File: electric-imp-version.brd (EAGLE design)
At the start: 32.1 x 50.8 mm, 44 parts, among them Q1 DMG2307L-7, U1 ELECTRIC_IMP, U2 TPS62172, U3 ATSHA204-TSU, U4 MCP73831, U5 CD74HC4067-SSOPCD74HC4067, U6 CD74HC4067-SSOPCD74HC4067, U7 LTC6904LTC6904, X1 USBSMD

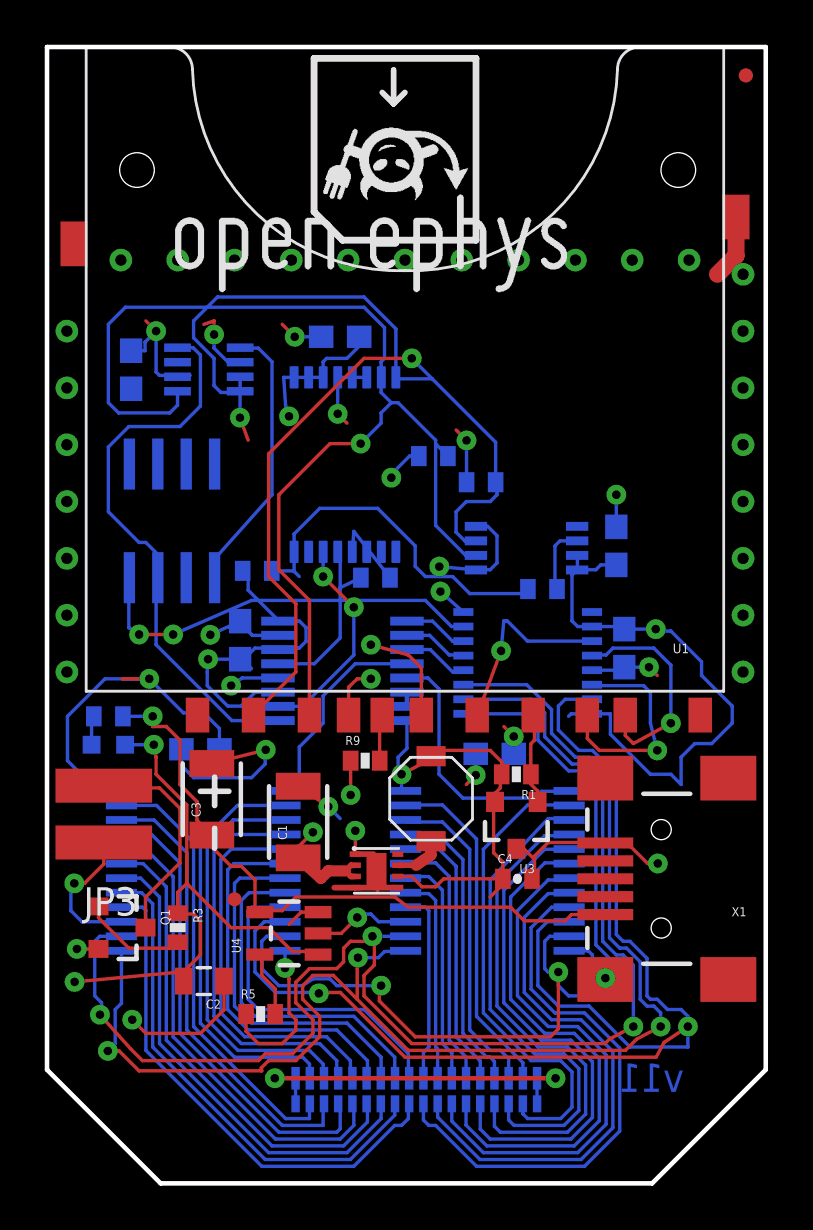
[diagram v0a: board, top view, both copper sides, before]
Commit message: Cleaning up traces
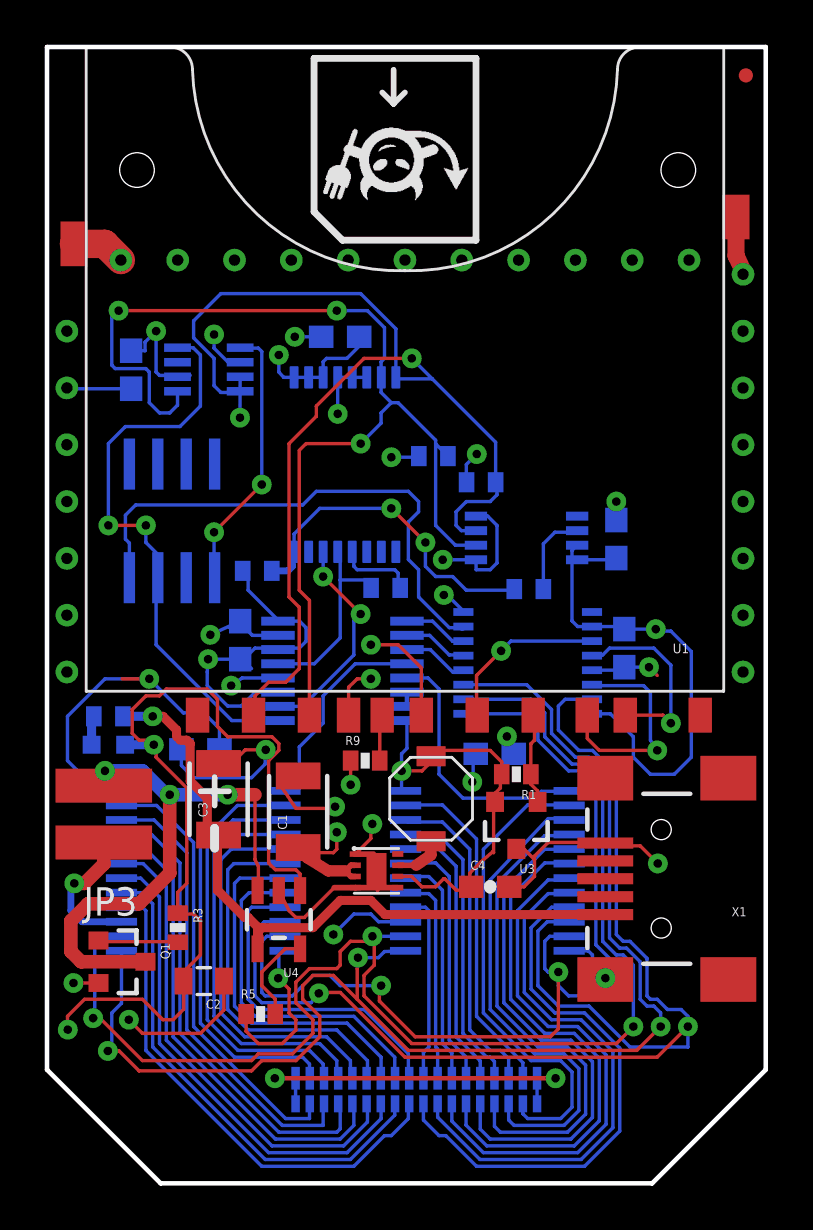
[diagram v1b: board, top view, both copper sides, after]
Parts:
- removed C13: 0.1uF, SparkFun-Capacitors:0603-CAP
- removed JP9: FIDUCIALUFIDUCIAL, SparkFun:MICRO-FIDUCIAL
- added C7: 0.1uF, SparkFun-Capacitors:0603-CAP
- C4: device SparkFun-Passives:0402-CAP -> SparkFun-Capacitors:0603-CAP
- R4: value 330k -> 330
- moved U$5 22.0 mm to (28.2, 28.9)
- moved U$7 20.5 mm to (25.0, 43.9), flipped to the bottom
- moved Q1 1.52 mm to (3.30, 9.91)
- moved C4 1.27 mm to (19.8, 13.3)
- moved U4 0.76 mm to (10.4, 11.8), turned to 180 degrees
- moved R8 0.65 mm to (15.1, 26.6)
- moved R2 0.61 mm to (21.5, 26.6)
- moved C1 0.46 mm to (11.2, 16.6)
- moved U7 0.46 mm to (21.4, 28.9)
- moved C3 0.30 mm to (7.67, 17.2)
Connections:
- net 3.3V: now also C7.1; no longer C13.1
- net GND: now also C7.2; no longer C13.2
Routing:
- net VBAT: track 11.3 -> 26.1 mm, vias 0 -> 3
- net N$9: track 15.2 -> 27.0 mm
- net GND: track 100.6 -> 112.3 mm
- net 3.3V: track 100.0 -> 90.4 mm
- net LM234EN: track 18.1 -> 23.8 mm, vias 2 -> 0
- net VUSB: track 28.9 -> 31.6 mm
- net N$6: track 2.94 -> 4.27 mm
- net VIN: track 22.7 -> 23.9 mm
- net CLOCK: track 16.1 -> 15.0 mm, vias 0 -> 2
- net MUX16_1: track 45.9 -> 47.0 mm
- net RCK: track 9.90 -> 8.76 mm
- net SCK: track 8.73 -> 7.68 mm
- net MUX16_0: track 57.1 -> 58.1 mm
- net CURRENT_SOURCE: track 25.9 -> 26.8 mm, vias 0 -> 2
- net SDA: track 51.2 -> 50.5 mm, vias 1 -> 3
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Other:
- board text added: "autoimpedance, v 2.0"
- board text removed: "GND"
- board text removed: "VIN"

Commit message: Fix layout
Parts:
- removed FRAME1: FRAME-LETTER, SparkFun-Aesthetics:CREATIVE_COMMONS
- moved U2 4.55 mm to (18.2, 11.1)
- moved JP3 3.61 mm to (5.74, 14.8)
- moved C3 2.76 mm to (10.4, 16.9)
- moved R3 2.75 mm to (6.76, 8.84), turned to 0 degrees
- moved C1 2.31 mm to (13.5, 16.9)
- moved L1 2.29 mm to (17.3, 14.9)
- moved C2 2.00 mm to (6.71, 7.06)
- moved Q1 1.84 mm to (3.45, 8.08)
- moved R9 1.59 mm to (15.7, 18.4), turned to 90 degrees
- moved C4 1.37 mm to (21.2, 13.3)
- moved C5 0.15 mm to (20.0, 19.1)
- moved U3 0.15 mm to (21.1, 16.1)
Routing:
- net N$9: track 27.0 -> 12.6 mm
- net VUSB: track 31.6 -> 39.4 mm
- net MUX16_2: track 61.1 -> 68.3 mm
- net MUX16_3: track 61.2 -> 66.7 mm
- net VBAT: track 26.1 -> 20.7 mm, vias 3 -> 0
- net MUX16_1: track 47.0 -> 52.1 mm
- net SCL: track 51.4 -> 54.8 mm
- net VIN: track 23.9 -> 26.7 mm
- net 3.3V: track 90.4 -> 93.2 mm, vias 13 -> 12
- net N$1: track 2.24 -> 4.38 mm
- net N$2: track 3.98 -> 5.96 mm
- net EIB_GND: track 37.1 -> 38.0 mm
- net SCK: track 7.68 -> 8.35 mm
- net GND: track 112.3 -> 112.8 mm, vias 45 -> 44
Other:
- board text added: "autoimpedance 2.0"
- board text removed: "autoimpedance, v 2.0"

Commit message: Aesthetic fixes
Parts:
- removed U4: MCP73831, SparkFun-PowerIC:SOT23-5
- added CHARGE: MCP73831, SparkFun-PowerIC:SOT23-5
- added FRAME1: FRAME-LETTER, SparkFun-Aesthetics:CREATIVE_COMMONS
- moved C7 0.84 mm to (26.3, 28.9)
- moved C3 0.24 mm to (10.6, 16.9)
- moved R6 0.23 mm to (19.2, 31.3)
- moved R5 0.17 mm to (9.40, 7.49)
- moved R8 0.08 mm to (15.1, 26.5)
- renumbered JP3 to JP1, S1 to OMNETICS, U$3 to IC1, U$4 to IC3, U$6 to IC2, U$8 to MUX3X2, U1 to SD, U2 to CONV, U3 to ID, U5 to MUX16A, U6 to MUX16B, U7 to CLK, U8 to SR, X1 to USB
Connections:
- net GND: now also CHARGE.2; no longer U4.2
- net N$6: now also CHARGE.5; no longer U4.5
- net N$9: now also CHARGE.1; no longer U4.1
- net VBAT: now also CHARGE.3; no longer U4.3
- net VUSB: now also CHARGE.4; no longer U4.4
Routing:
- net SDA: track 50.5 -> 44.3 mm
- net 3.3V: track 93.2 -> 95.4 mm
- net VIN: track 26.7 -> 28.2 mm
- net TEST_OUT: track 9.77 -> 11.1 mm
- net VUSB: track 39.4 -> 38.4 mm
- net CLOCK: track 15.0 -> 15.6 mm

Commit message: Aesthetic fixes
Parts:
- moved U$5 32.2 mm to (6.76, 4.90)
- moved Q1 0.61 mm to (2.84, 8.08)
- moved C2 0.46 mm to (6.25, 7.06)
- moved R1 0.30 mm to (21.0, 18.6)
- moved R3 0.15 mm to (6.76, 8.99)
- moved C4 0.08 mm to (21.2, 13.2)
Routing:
- net N$2: track 5.96 -> 6.96 mm
- net GND: track 112.9 -> 113.9 mm
- net 3.3V: track 95.4 -> 96.2 mm
- net VBAT: track 20.9 -> 21.4 mm

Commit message: Fix LM234 channel mapping
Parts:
- removed IC2: LM234, josh:LM234
- added U$2: LM234, josh:LM234
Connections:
- net CURRENT_SOURCE: now also U$2.6; no longer IC2.3
- net LM234EN: now also U$2.4; no longer IC2.4
- net W: now also U$2.1; no longer IC2.1
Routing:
- net CURRENT_SOURCE: track 27.1 -> 30.4 mm, vias 2 -> 0
- net W: track 12.1 -> 13.8 mm
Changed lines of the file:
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@@
 <grid distance="0.003" unitdist="inch" unit="inch" style="lines" multiple="1" display="yes" altdistance="0.005" altunitdist="inch" altunit="inch"/>
 <layers>
-<layer number="1" name="Top" color="4" fill="1" visible="no" active="yes"/>
+<layer number="1" name="Top" color="4" fill="1" visible="yes" active="yes"/>
 <layer number="2" name="Route2" color="11" fill="1" visible="no" active="yes"/>
 <layer number="3" name="Route3" color="8" fill="1" visible="no" active="yes"/>
@@
 <layer number="17" name="Pads" color="2" fill="1" visible="yes" active="yes"/>
 <layer number="18" name="Vias" color="2" fill="1" visible="yes" active="yes"/>
-<layer number="19" name="Unrouted" color="14" fill="1" visible="yes" active="yes"/>
+<layer number="19" name="Unrouted" color="15" fill="1" visible="yes" active="yes"/>
 <layer number="20" name="Dimension" color="15" fill="1" visible="yes" active="yes"/>
 <layer number="21" name="tPlace" color="3" fill="1" visible="no" active="yes"/>
 <layer number="22" name="bPlace" color="5" fill="1" visible="yes" active="yes"/>
-<layer number="23" name="tOrigins" color="15" fill="1" visible="no" active="yes"/>
+<layer number="23" name="tOrigins" color="15" fill="1" visible="yes" active="yes"/>
 <layer number="24" name="bOrigins" color="15" fill="1" visible="yes" active="yes"/>
 <layer number="25" name="tNames" color="3" fill="1" visible="no" active="yes"/>
@@
 <attribute name="VALUE" x="10.7569" y="6.9596" size="0.4064" layer="27" font="vector" ratio="10"/>
 </element>
-<element name="IC2" library="josh" package="LM234" value="LM234" x="5.588" y="29.6164" rot="MR0"/>
 <element name="R6" library="SparkFun-Passives" package="0402-RES" value="4.7k" x="19.177" y="31.3436" smashed="yes" rot="MR0">
 <attribute name="NAME" x="20.1422" y="31.9659" size="0.4064" layer="26" font="vector" ratio="10" rot="MR0"/>
@@
 </element>
 <element name="FRAME1" library="SparkFun-Aesthetics" package="CREATIVE_COMMONS" value="FRAME-LETTER" x="-3.7338" y="-11.7348"/>
+<element name="U$2" library="josh" package="LM234" value="LM234" x="4.7244" y="29.4132" rot="MR0"/>
 </elements>
 <signals>
@@
 </signal>
 <signal name="LM234EN">
-<contactref element="IC2" pad="4"/>
 <contactref element="SR" pad="7"/>
-<wire x1="3.683" y1="27.0764" x2="3.683" y2="28.6258" width="0.1524" layer="16"/>
-<wire x1="3.683" y1="28.6258" x2="3.5052" y2="28.8036" width="0.1524" layer="16"/>
-<wire x1="3.5052" y1="28.8036" x2="3.5052" y2="29.8704" width="0.1524" layer="16"/>
-<wire x1="3.5052" y1="29.8704" x2="3.9624" y2="30.3276" width="0.1524" layer="16"/>
 <wire x1="3.9624" y1="30.3276" x2="11.43" y2="30.3276" width="0.1524" layer="16"/>
 <wire x1="11.43" y1="30.3276" x2="12.0396" y2="30.9372" width="0.1524" layer="16"/>
@@
 <wire x1="17.9832" y1="24.8412" x2="18.5632" y2="24.8412" width="0.1524" layer="16"/>
 <wire x1="18.5632" y1="24.8412" x2="18.6134" y2="24.8914" width="0.1524" layer="16"/>
+<contactref element="U$2" pad="4"/>
+<wire x1="3.9624" y1="30.3276" x2="2.8956" y2="29.2608" width="0.1524" layer="16"/>
+<wire x1="2.8956" y1="29.2608" x2="2.8956" y2="26.9494" width="0.1524" layer="16"/>
+<wire x1="2.8956" y1="26.9494" x2="2.8194" y2="26.8732" width="0.1524" layer="16"/>
 </signal>
 <signal name="W">
 <contactref element="IC3" pad="1"/>
-<contactref element="IC2" pad="1"/>
-<wire x1="7.493" y1="27.0764" x2="7.493" y2="27.9146" width="0.1524" layer="16"/>
-<wire x1="7.493" y1="27.9146" x2="7.4676" y2="27.8892" width="0.1524" layer="16"/>
-<wire x1="7.4676" y1="27.8892" x2="7.4676" y2="29.1084" width="0.1524" layer="16"/>
-<wire x1="7.4676" y1="29.1084" x2="9.6012" y2="31.242" width="0.3048" layer="1"/>
+<wire x1="7.5438" y1="29.4894" x2="9.6012" y2="29.4894" width="0.1524" layer="16"/>
+<wire x1="9.6012" y1="29.4894" x2="9.6012" y2="31.242" width="0.3048" layer="1"/>
 <wire x1="9.6012" y1="31.242" x2="9.6012" y2="37.1856" width="0.1524" layer="16"/>
 <wire x1="9.6012" y1="37.1856" x2="9.4488" y2="37.338" width="0.1524" layer="16"/>
 <wire x1="9.4488" y1="37.338" x2="8.655" y2="37.338" width="0.1524" layer="16"/>
 <wire x1="8.655" y1="37.338" x2="8.6344" y2="37.3586" width="0.1524" layer="16"/>
-<via x="7.4676" y="29.1084" extent="1-16" drill="0.381"/>
+<via x="9.6012" y="29.4894" extent="1-16" drill="0.381"/>
 <via x="9.6012" y="31.242" extent="1-16" drill="0.381"/>
+<contactref element="U$2" pad="1"/>
+<wire x1="6.6294" y1="26.8732" x2="6.6294" y2="28.575" width="0.1524" layer="16"/>
+<wire x1="6.6294" y1="28.575" x2="7.5438" y2="29.4894" width="0.1524" layer="16"/>
 </signal>
 <signal name="CURRENT_SOURCE">
 <contactref element="IC3" pad="8"/>
-<contactref element="IC2" pad="3"/>
 <contactref element="MUX3X2" pad="1"/>
 <wire x1="10.3251" y1="20.6883" x2="7.8105" y2="20.6883" width="0.1524" layer="16"/>
 <wire x1="7.8105" y1="20.6883" x2="4.8768" y2="23.622" width="0.1524" layer="16"/>
-<wire x1="4.8768" y1="23.622" x2="4.8768" y2="26.543" width="0.1524" layer="16"/>
-<wire x1="4.8768" y1="26.543" x2="4.953" y2="27.0764" width="0.1524" layer="16"/>
 <wire x1="5.8344" y1="37.3586" x2="6.5326" y2="37.3586" width="0.1524" layer="16"/>
 <wire x1="6.5326" y1="37.3586" x2="6.858" y2="37.0332" width="0.1524" layer="16"/>
 <wire x1="6.858" y1="37.0332" x2="6.858" y2="34.7472" width="0.1524" layer="16"/>
 <wire x1="6.858" y1="34.7472" x2="5.9436" y2="33.8328" width="0.1524" layer="16"/>
-<wire x1="5.9436" y1="33.8328" x2="3.5052" y2="33.8328" width="0.1524" layer="16"/>
-<wire x1="3.5052" y1="33.8328" x2="2.7432" y2="33.0708" width="0.1524" layer="16"/>
-<wire x1="2.7432" y1="33.0708" x2="2.7432" y2="29.4132" width="0.1524" layer="16"/>
-<wire x1="2.7432" y1="29.4132" x2="4.4196" y2="29.4132" width="0.3048" layer="1"/>
-<wire x1="4.4196" y1="29.4132" x2="4.4196" y2="28.6512" width="0.1524" layer="16"/>
-<wire x1="4.4196" y1="28.6512" x2="5.0292" y2="28.0416" width="0.1524" layer="16"/>
-<wire x1="5.0292" y1="28.0416" x2="5.0292" y2="26.6954" width="0.1524" layer="16"/>
-<wire x1="5.0292" y1="26.6954" x2="4.953" y2="27.0764" width="0.1524" layer="16"/>
-<via x="2.7432" y="29.4132" extent="1-16" drill="0.381"/>
-<via x="4.4196" y="29.4132" extent="1-16" drill="0.381"/>
+<contactref element="U$2" pad="6"/>
+<wire x1="4.8768" y1="23.622" x2="3.7338" y2="23.622" width="0.1524" layer="16"/>
+<wire x1="3.7338" y1="23.622" x2="2.1336" y2="25.2222" width="0.1524" layer="16"/>
+<wire x1="2.1336" y1="25.2222" x2="2.1336" y2="33.4518" width="0.1524" layer="16"/>
+<wire x1="2.1336" y1="33.4518" x2="2.5146" y2="33.8328" width="0.1524" layer="16"/>
+<wire x1="5.9436" y1="33.8328" x2="4.4196" y2="33.8328" width="0.1524" layer="16"/>
+<wire x1="4.4196" y1="33.8328" x2="4.1148" y2="33.528" width="0.1524" layer="16"/>
+<wire x1="4.1148" y1="33.528" x2="4.1148" y2="32.6136" width="0.1524" layer="16"/>
+<wire x1="4.1148" y1="32.6136" x2="4.0386" y2="32.5374" width="0.1524" layer="16"/>
+<wire x1="4.0386" y1="32.5374" x2="4.0386" y2="32.004" width="0.1524" layer="16"/>
+<wire x1="4.0386" y1="32.004" x2="4.0894" y2="31.9532" width="0.1524" layer="16"/>
+<wire x1="4.0894" y1="31.9532" x2="4.0894" y2="33.4772" width="0.1524" layer="16"/>
+<wire x1="4.0894" y1="33.4772" x2="3.7338" y2="33.8328" width="0.1524" layer="16"/>
+<wire x1="3.7338" y1="33.8328" x2="2.5146" y2="33.8328" width="0.1524" layer="16"/>
 </signal>
 <signal name="N$3">

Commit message: Update BOM
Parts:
- renumbered U$2 to IC2
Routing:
- net SCL: track 54.7 -> 55.5 mm
- net VUSB: track 38.4 -> 39.2 mm
